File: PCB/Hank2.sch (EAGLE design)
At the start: 100 parts, among them T1 2n2222, T2 2n2222, T3 2n2222, T4 2n2222, T5 2n2222, T6 2n2222, T7 2n2222, T8 2n2222, X3 Auto_Manual

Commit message: Changed v-regs and updated arduino program ready to test the ssrs
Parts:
- removed LF33CV, LF50ABV: (no value), v-reg:78XXL
- added IC1: LP2950CDT-3.3, v-reg:LP2950CDT-3.3
- added IC2: LP2950CDT-5.0, v-reg:LP2950CDT-5.0
- added NI1: 1k, rcl:R-US_0204/7
- added NI2: 2K, rcl:R-US_0204/7
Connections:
- new net N$32: ARDUINO.28, NI1.2
- new net NEW_IN: NI1.1, NI2.1, SV1.6
- net +3V3: now also IC1.OUT; no longer LF33CV.OUT
- net +5V: now also IC2.OUT; no longer LF50ABV.OUT
- net CP12: now also IC1.IN, IC2.IN; no longer LF33CV.IN, LF50ABV.IN
- net GND: now also IC1.GND, IC2.GND, NI2.2; no longer LF33CV.GND, LF50ABV.GND, SV1.6
- net N$12: now also T5.C; no longer T8.C
- net N$17: now also T6.C; no longer T7.C
- net N$18: now also T6.B; no longer T7.B
- net N$21: now also T7.C; no longer T6.C
- net N$22: now also T7.B; no longer T6.B
- net N$26: now also T8.C; no longer T5.C
- net N$34: now also T8.B; no longer T5.B
- net N$9: now also T5.B; no longer T8.B
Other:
- moved on the sheet: T5, T6, T7, T8

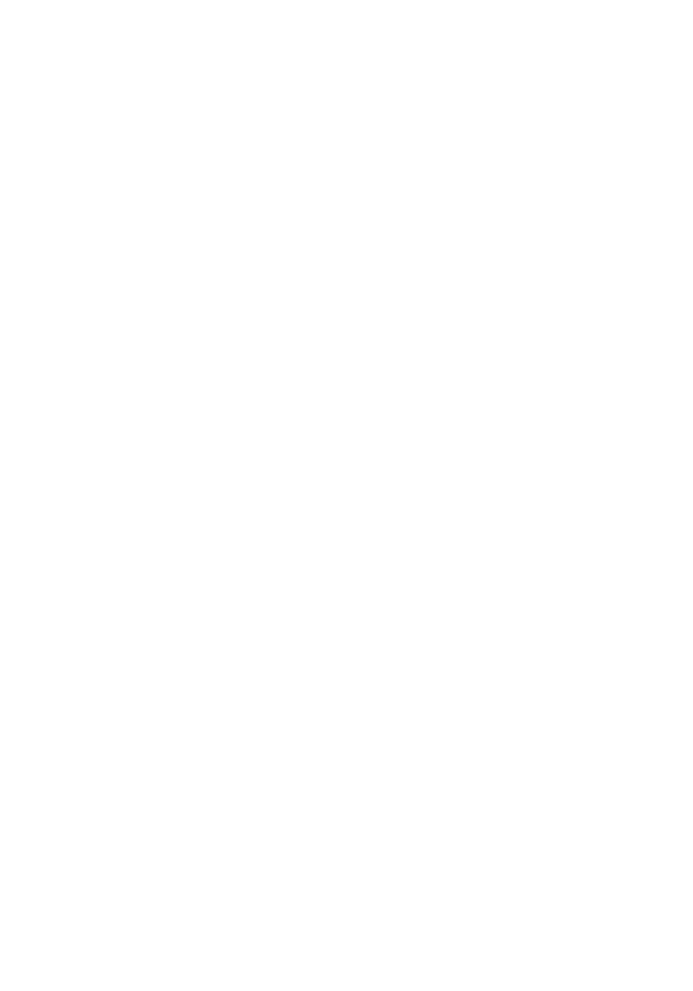
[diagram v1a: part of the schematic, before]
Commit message: Tested the Atmega 328P and is fit for porpuse, Also got the Eagle library to add the Ic in the PCB
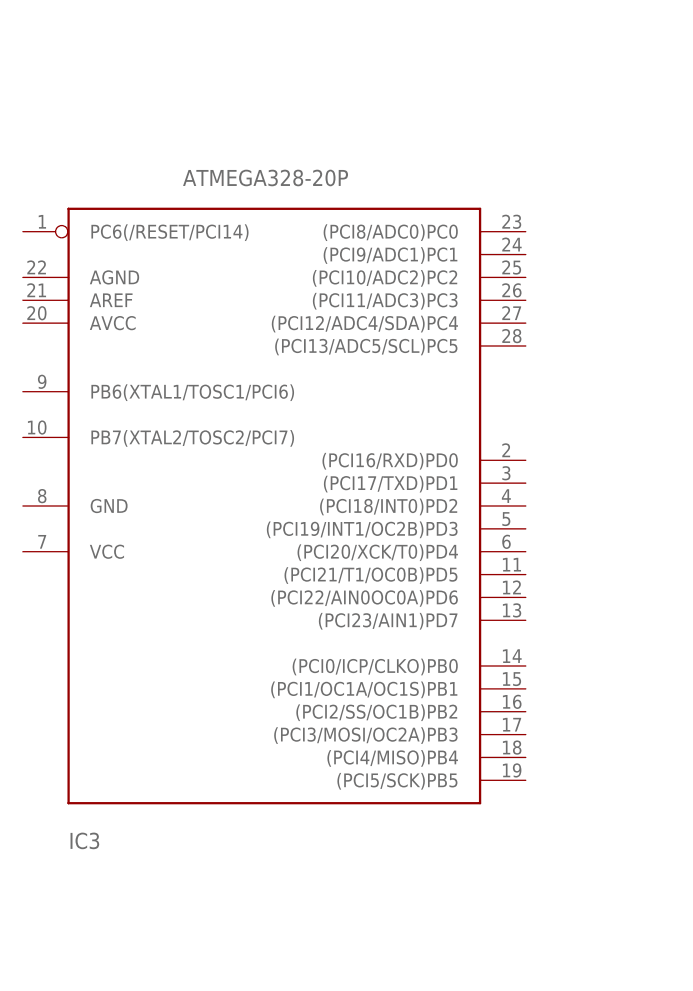
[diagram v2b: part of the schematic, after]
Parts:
- added IC3: ATMEGA328-20P, atmega328:ATMEGA328-20P
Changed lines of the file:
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@@
 <layer number="54" name="bGND_GNDA" color="1" fill="9" visible="no" active="no"/>
 <layer number="56" name="wert" color="7" fill="1" visible="no" active="no"/>
+<layer number="57" name="tCAD" color="7" fill="1" visible="no" active="no"/>
 <layer number="88" name="SimResults" color="9" fill="1" visible="yes" active="yes"/>
 <layer number="89" name="SimProbes" color="9" fill="1" visible="yes" active="yes"/>
@@
 <layer number="106" name="bPlate" color="7" fill="1" visible="yes" active="yes"/>
 <layer number="107" name="Crop" color="7" fill="1" visible="yes" active="yes"/>
+<layer number="108" name="fp8" color="7" fill="1" visible="no" active="yes"/>
+<layer number="109" name="fp9" color="7" fill="1" visible="no" active="yes"/>
+<layer number="110" name="fp0" color="7" fill="1" visible="no" active="yes"/>
+<layer number="111" name="LPC17xx" color="7" fill="1" visible="yes" active="yes"/>
+<layer number="112" name="tSilk" color="7" fill="1" visible="yes" active="yes"/>
 <layer number="116" name="Patch_BOT" color="9" fill="4" visible="yes" active="yes"/>
 <layer number="121" name="_tsilk" color="7" fill="1" visible="yes" active="yes"/>
 <layer number="122" name="_bsilk" color="7" fill="1" visible="yes" active="yes"/>
+<layer number="123" name="tTestmark" color="7" fill="1" visible="no" active="yes"/>
+<layer number="124" name="bTestmark" color="7" fill="1" visible="no" active="yes"/>
+<layer number="125" name="_tNames" color="7" fill="1" visible="yes" active="yes"/>
+<layer number="126" name="_bNames" color="7" fill="1" visible="yes" active="yes"/>
+<layer number="127" name="_tValues" color="7" fill="1" visible="yes" active="yes"/>
+<layer number="128" name="_bValues" color="7" fill="1" visible="yes" active="yes"/>
+<layer number="131" name="tAdjust" color="7" fill="1" visible="no" active="yes"/>
+<layer number="132" name="bAdjust" color="7" fill="1" visible="no" active="yes"/>
 <layer number="144" name="Drill_legend" color="7" fill="1" visible="yes" active="yes"/>
+<layer number="150" name="Notes" color="7" fill="1" visible="no" active="yes"/>
 <layer number="151" name="HeatSink" color="7" fill="1" visible="yes" active="yes"/>
+<layer number="152" name="_bDocu" color="7" fill="1" visible="yes" active="yes"/>
+<layer number="153" name="FabDoc1" color="6" fill="1" visible="no" active="no"/>
+<layer number="154" name="FabDoc2" color="2" fill="1" visible="no" active="no"/>
+<layer number="155" name="FabDoc3" color="7" fill="15" visible="no" active="no"/>
+<layer number="199" name="Contour" color="7" fill="1" visible="yes" active="yes"/>
 <layer number="200" name="200bmp" color="1" fill="10" visible="no" active="no"/>
 <layer number="201" name="201bmp" color="2" fill="1" visible="no" active="no"/>
@@
 <layer number="215" name="215bmp" color="7" fill="1" visible="yes" active="yes"/>
 <layer number="216" name="216bmp" color="7" fill="1" visible="yes" active="yes"/>
+<layer number="217" name="217bmp" color="18" fill="1" visible="no" active="no"/>
+<layer number="218" name="218bmp" color="19" fill="1" visible="no" active="no"/>
+<layer number="219" name="219bmp" color="20" fill="1" visible="no" active="no"/>
+<layer number="220" name="220bmp" color="21" fill="1" visible="no" active="no"/>
+<layer number="221" name="221bmp" color="22" fill="1" visible="no" active="no"/>
+<layer number="222" name="222bmp" color="23" fill="1" visible="no" active="no"/>
+<layer number="223" name="223bmp" color="24" fill="1" visible="no" active="no"/>
+<layer number="224" name="224bmp" color="25" fill="1" visible="no" active="no"/>
+<layer number="248" name="Housing" color="7" fill="1" visible="yes" active="yes"/>
+<layer number="249" name="Edge" color="7" fill="1" visible="yes" active="yes"/>
 <layer number="250" name="Descript" color="3" fill="1" visible="no" active="no"/>
 <layer number="251" name="SMDround" color="12" fill="11" visible="no" active="no"/>
@@
 <part name="IC1" library="v-reg" deviceset="LP2950?*" device="CDT" technology="-3.3"/>
 <part name="IC2" library="v-reg" deviceset="LP2950?*" device="CDT" technology="-5.0"/>
+<part name="IC3" library="atmega328" deviceset="ATMEGA328*P" device="" technology="-20"/>
 </parts>
 <sheets>
@@
 <instance part="IC1" gate="G$1" x="53.34" y="68.58"/>
 <instance part="IC2" gate="G$1" x="53.34" y="33.02"/>
+<instance part="IC3" gate="G$1" x="-45.72" y="60.96"/>
 </instances>
 <busses>

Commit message: Added Atmega 328-20P to the pcb and wired, still to be verified and tidied up
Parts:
- removed ARDUINO: ARDUINO_MICRO, HankLibraries:ARDUINO_MICRO
- added C_RTC1, C_USD1, C_USD2, C_USD3: 0.1uF, rcl:C-US025-024X044
- added D1: 1N4148DO35-7, diode:1N4148DO35-7
- added FTDI: (no value), con-lstb:MA06-1
- added Q1: 16M, crystal:CRYSTALHC49S
- added RDX: 10k, rcl:R-US_0204/7
- added RI9: 330, rcl:R-US_0204/7
- added S1: DTE6, switch-misc:DTE6
- added SV4: (no value), con-lstb:MA03-2
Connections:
- removed net ARD_RX: ARDUINO.20
- removed net ARD_TX: TX1.1, TX2.2
- new net N$35: C_USD2.1, IC3.PB7(XTAL2/TOSC2/PCI7), Q1.1
- new net N$39: IC3.(PCI2/SS/OC1B)PB2, NI1.2
- new net RTS: C_RTC1.1, FTDI.6
- new net RXD: RDX.2
- new net TXD: FTDI.4
- new net U_RESET: C_RTC1.2, D1.A, IC3.PC6(/RESET/PCI14), RI9.2, S1.S, S1.S@1, SV4.5
- new net U_RX: IC3.(PCI16/RXD)PD0, SV1.7
- new net U_TX: IC3.(PCI17/TXD)PD1, TX1.2
- new net U_TX_3: SV1.8, TX1.1, TX2.2
- net +5V: now also C_USD3.2, D1.C, FTDI.3, IC3.AREF, IC3.AVCC, IC3.VCC, RI9.1, SV4.2; no longer ARDUINO.VIN
- net AUTO_MANUAL: now also IC3.(PCI3/MOSI/OC2A)PB3, SV4.4; no longer ARDUINO.10
- net GND: now also C_USD1.2, C_USD2.2, C_USD3.1, FTDI.1, FTDI.2, IC3.AGND, IC3.GND, S1.P, S1.P@1, SV4.6, T4.E, T8.E; no longer ARDUINO.GND1, ARDUINO.GND2
- net IN1: now also IC3.(PCI8/ADC0)PC0; no longer ARDUINO.36
- net IN2: now also IC3.(PCI9/ADC1)PC1; no longer ARDUINO.37
- net IN3: now also IC3.(PCI10/ADC2)PC2; no longer ARDUINO.38
- net IN4: now also IC3.(PCI11/ADC3)PC3; no longer ARDUINO.39
- net IN5: now also IC3.(PCI12/ADC4/SDA)PC4; no longer ARDUINO.40
- net IN6: now also IC3.(PCI13/ADC5/SCL)PC5; no longer ARDUINO.41
- net IN7: now also IC3.(PCI4/MISO)PB4, SV4.1; no longer ARDUINO.11
- net IN8: now also IC3.(PCI5/SCK)PB5, SV4.3; no longer ARDUINO.9
- net N$32: now also C_USD1.1, IC3.PB6(XTAL1/TOSC1/PCI6), Q1.2; no longer ARDUINO.28, NI1.2
- net N$6: now also FTDI.5, RDX.1; no longer ARDUINO.21, TX1.2
- net OUT1: now also IC3.(PCI18/INT0)PD2; no longer ARDUINO.32
- net OUT2: now also IC3.(PCI19/INT1/OC2B)PD3; no longer ARDUINO.26
- net OUT3: now also IC3.(PCI20/XCK/T0)PD4; no longer ARDUINO.12
- net OUT4: now also IC3.(PCI21/T1/OC0B)PD5; no longer ARDUINO.30
- net OUT5: now also IC3.(PCI22/AIN0OC0A)PD6; no longer ARDUINO.29
- net OUT6: now also IC3.(PCI23/AIN1)PD7; no longer ARDUINO.27
- net OUT7: now also IC3.(PCI0/ICP/CLKO)PB0; no longer ARDUINO.31
- net OUT8: now also IC3.(PCI1/OC1A/OC1S)PB1; no longer ARDUINO.18
- net SERIAL_RXD: no longer SV1.7
- net SERIAL_TXD: no longer SV1.8
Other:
- note added: "/RESET"
- note added: "CTS"
- note added: "GND"
- note added: "MISO"
- note added: "MOSI"
- note added: "RTS"
- note added: "RXD"
- note added: "SCK"
- note added: "TO DO: +DONE Add connections to Microcontroller -Add 3.3V Power Supply Regulator -Add 5V low drop regulator +DONE: Add Temperature Sensor +DONE: Add the SSR Circuit -DONE:Add Fuses SM 092 A0 2A--- RS PN: 116-114 -Add Connector with 8Inputs http://www.gammon.com.au/images/Wire_Wrapped_Atmega132_e.png"
- note added: "TXD"
- note added: "VCC"
- note removed: "TO DO: +DONE Add connections to Microcontroller -Add 3.3V Power Supply Regulator -Add 5V low drop regulator +DONE: Add Temperature Sensor +DONE: Add the SSR Circuit -DONE:Add Fuses SM 092 A0 2A--- RS PN: 116-114 -Add Connector with 8Inputs"
- moved on the sheet: 3.3V, 5V, CP01, CP02, CP31, CP32, CP51, CP52, F4, F8, IC1, IC2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

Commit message: Started arranging components in the PCB
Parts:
- removed 3.3V, 5V: (no value), led:LED3MM
- removed C_RTC1, C_USD1, C_USD2, C_USD3: 0.1uF, rcl:C-US025-024X044
- removed D1: 1N4148DO35-7, diode:1N4148DO35-7
- removed IC1: LP2950CDT-3.3, v-reg:LP2950CDT-3.3
- removed IC2: LP2950CDT-5.0, v-reg:LP2950CDT-5.0
- removed JUM_3.3V, JUM_5.5V: 22-23-2021, con-molex:22-23-2021
- removed MOUT: (no value), con-ptr500:AK300/10
- removed NI1, TX1: 1k, rcl:R-US_0204/7
- removed NI2, TX2: 2K, rcl:R-US_0204/7
- removed Q1: 16M, crystal:CRYSTALHC49S
- removed R2: (no value), rcl:R-US_0204/7
- removed RI9: 330, rcl:R-US_0204/7
- removed S1: DTE6, switch-misc:DTE6
- removed X3: Auto_Manual, con-molex:22-23-2021
- added AUTO: Auto_Manual, con-molex:22-23-2021
- added C_U, C_URTS, C_UXTAL1, C_UXTAL2: 0.1uF, rcl:C-US025-024X044
- added D_3V3, D_5V: (no value), led:LED3MM
- added D_URES: 1N4148DO35-7, diode:1N4148DO35-7
- added J_3.3V, J_5.5V: Jumper, con-molex:22-23-2021
- added REG_3V3: LP2950CDT-3.3, v-reg:LP2950CDT-3.3
- added REG_5V: LP2950CDT-5.0, v-reg:LP2950CDT-5.0
- added R_AUTO: (no value), rcl:R-US_0204/7
- added R_NI1, R_UTX1: 1k, rcl:R-US_0204/7
- added R_NI2, R_UTX2: 2K, rcl:R-US_0204/7
- added R_URES: 330, rcl:R-US_0204/7
- added URES: DTE6, switch-misc:DTE6
- added X1, X2: (no value), con-ptr500:AK300/5
- added XTALU: 16M, crystal:CRYSTALHC49S
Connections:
- removed net N$14: SV1.10
- net +3V3: now also AUTO-1.S, D_3V3.A, J_5.5V-1.S, REG_3V3.OUT; no longer 3.3V.A, IC1.OUT, JUM_5.5V-1.S, X3-1.S
- net +5V: now also C_U.2, D_5V.A, D_URES.C, J_3.3V-1.S, REG_5V.OUT, R_URES.1; no longer 5V.A, C_USD3.2, D1.C, IC2.OUT, JUM_3.3V-1.S, RI9.1
- net AUTO_MANUAL: now also AUTO-2.S, R_AUTO.2; no longer R2.2, X3-2.S
- net CP12: now also REG_3V3.IN, REG_5V.IN; no longer IC1.IN, IC2.IN
- net GND: now also C_U.1, C_UXTAL1.2, C_UXTAL2.2, REG_3V3.GND, REG_5V.GND, R_AUTO.1, R_NI2.2, R_UTX2.1, T1.E, T2.E, T5.E, T6.E, T7.E, URES.P, URES.P@1; no longer C_USD1.2, C_USD2.2, C_USD3.1, IC1.GND, IC2.GND, NI2.2, R2.1, S1.P, S1.P@1, TX2.1
- net L1-1: now also X1-5.KL; no longer MOUT-1.KL
- net L1-2: now also X2-5.KL; no longer MOUT-6.KL
- net MO1: now also X1-1.KL; no longer MOUT-2.KL
- net MO2: now also X1-2.KL; no longer MOUT-3.KL
- net MO3: now also X1-3.KL; no longer MOUT-4.KL
- net MO4: now also X1-4.KL; no longer MOUT-5.KL
- net MO5: now also X2-1.KL; no longer MOUT-7.KL
- net MO6: now also X2-2.KL; no longer MOUT-8.KL
- net MO7: now also X2-3.KL; no longer MOUT-9.KL
- net MO8: now also X2-4.KL; no longer MOUT-10.KL
- net N$1: now also J_3.3V-2.S; no longer JUM_3.3V-2.S
- net N$2: now also J_5.5V-2.S; no longer JUM_5.5V-2.S
- net N$32: now also C_UXTAL1.1, XTALU.2; no longer C_USD1.1, Q1.2
- net N$35: now also C_UXTAL2.1, XTALU.1; no longer C_USD2.1, Q1.1
- net N$39: now also R_NI1.2; no longer NI1.2
- net N$4: now also D_5V.C; no longer 5V.C
- net N$5: now also D_3V3.C; no longer 3.3V.C
- net NEW_IN: now also R_NI1.1, R_NI2.1; no longer NI1.1, NI2.1
- net RTS: now also C_URTS.1; no longer C_RTC1.1
- net SCL: now also SV1.10
- net SDA: now also SV1.9
- net U_RESET: now also C_URTS.2, D_URES.A, R_URES.2, URES.S, URES.S@1; no longer C_RTC1.2, D1.A, RI9.2, S1.S, S1.S@1
- net U_TX: now also R_UTX1.2; no longer TX1.2
- net U_TX_3: now also R_UTX1.1, R_UTX2.2; no longer TX1.1, TX2.2
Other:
- moved on the sheet: CP01, CP02, CP31, CP32, CP51, CP52, C_BT, C_FM, C_OLED, C_RTC, C_USD, F1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

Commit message: Added parts schedule
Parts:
- IN_BUTTONS: value (none) -> User Inputs
- RI8, R_AUTO: value (none) -> 330
- RO33: value (none) -> 1k
- X1: value (none) -> Sockets 1
- X2: value (none) -> Sockets 2
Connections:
- removed net N$10: U$4.KEY
- removed net N$13: U$4.5V
- removed net N$15: R51.2, RO52.2
- removed net N$19: R61.2, RO62.2
- removed net N$24: RO71.2, RO72.2
- removed net N$28: RO81.2, RO82.2
- removed net N$36: RO21.2, RO22.2
- removed net N$40: RO31.2, RO32.2
- removed net N$44: RO41.2, RO42.2
- removed net N$7: RI1.2, RI2.2, RI3.2, RI4.2, RI5.2, RI6.2, RI7.2, RI8.2
- removed net RXD: RDX.2
- removed net SERIAL_RXD: U$4.RXD
- removed net SERIAL_TXD: U$4.TXD
- removed net TXD: FTDI.4
- new net BT_RX: SV1.4, U$4.RXD
- new net BT_TX: SV1.5, U$4.TXD
- net GND: now also RI1.2, RI2.2, RI3.2, RI4.2, RI5.2, RI6.2, RI7.2, RI8.2; no longer SV1.4, SV1.5
- net IN1: now also IC3.(PCI4/MISO)PB4, IN_BUTTONS.9, RI8.1; no longer IC3.(PCI8/ADC0)PC0, IN_BUTTONS.2, RI1.1
- net IN2: now also IC3.(PCI5/SCK)PB5, IN_BUTTONS.8, RI7.1; no longer IC3.(PCI9/ADC1)PC1, IN_BUTTONS.3, RI2.1
- net IN3: now also IC3.(PCI8/ADC0)PC0, IN_BUTTONS.7, RI6.1; no longer IC3.(PCI10/ADC2)PC2, IN_BUTTONS.4, RI3.1
- net IN4: now also IC3.(PCI9/ADC1)PC1, IN_BUTTONS.6, RI5.1; no longer IC3.(PCI11/ADC3)PC3, IN_BUTTONS.5, RI4.1
- net IN5: now also IC3.(PCI10/ADC2)PC2, IN_BUTTONS.5, RI4.1; no longer IC3.(PCI12/ADC4/SDA)PC4, IN_BUTTONS.6, RI5.1
- net IN6: now also IC3.(PCI11/ADC3)PC3, IN_BUTTONS.4, RI3.1; no longer IC3.(PCI13/ADC5/SCL)PC5, IN_BUTTONS.7, RI6.1
- net IN7: now also IC3.(PCI12/ADC4/SDA)PC4, IN_BUTTONS.3, RI2.1; no longer IC3.(PCI4/MISO)PB4, IN_BUTTONS.8, RI7.1
- net IN8: now also IC3.(PCI13/ADC5/SCL)PC5, IN_BUTTONS.2, RI1.1; no longer IC3.(PCI5/SCK)PB5, IN_BUTTONS.9, RI8.1
- net OUT2: now also RO21.2, RO22.2
- net OUT3: now also RO31.2, RO32.2
- net OUT4: now also RO41.2, RO42.2
- net OUT5: now also R51.2, RO52.2
- net OUT6: now also R61.2, RO62.2
- net OUT7: now also RO71.2, RO72.2
- net OUT8: now also RO81.2, RO82.2
- net U_RX: now also FTDI.4
- net U_TX: now also RDX.2
